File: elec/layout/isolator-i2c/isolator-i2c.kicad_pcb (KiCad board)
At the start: 2 copper layers, 7 parts, among them U1 10kΩ ±1% 62.5mW, U2 10kΩ ±1% 62.5mW, U4 10kΩ ±1% 62.5mW, U5 10kΩ ±1% 62.5mW, U6 100nF ±10% 16V X7R, U7 100nF ±10% 16V X7R

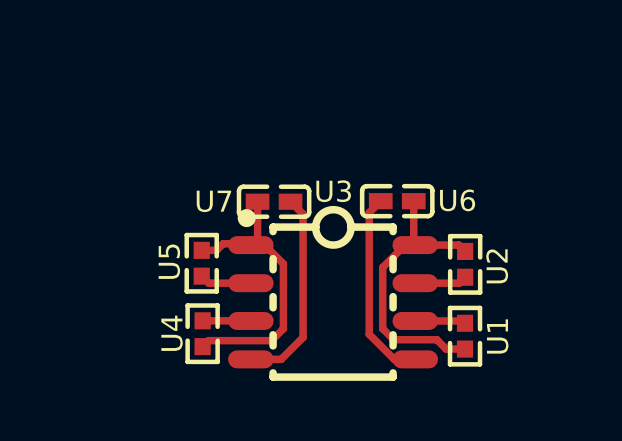
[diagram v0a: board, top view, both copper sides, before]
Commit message: remove default build, build everything locally
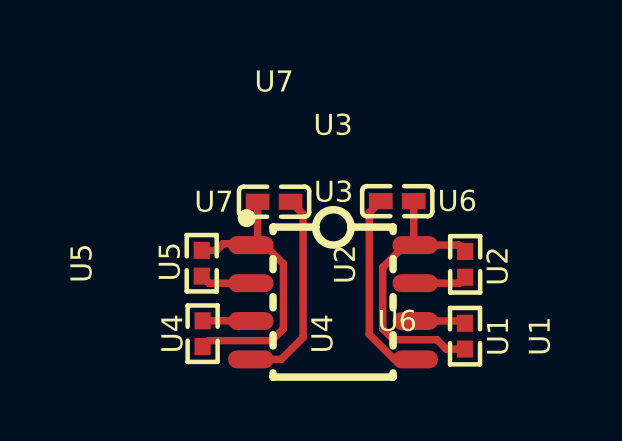
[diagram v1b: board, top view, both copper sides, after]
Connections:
- net scl renamed line-2
- net scl-1 renamed line-1
- net sda renamed line-3
- net sda-1 renamed line
- U1 pad 2: hv-1 -> hv
- U2 pad 2: hv-1 -> hv
- U3 pad 1: hv -> hv-1
- U3 pad 4: gnd -> gnd-1
- U3 pad 5: gnd-1 -> gnd
- U3 pad 8: hv-1 -> hv
- U4 pad 2: hv -> hv-1
- U5 pad 2: hv -> hv-1
- U6 pad 1: hv-1 -> hv
- U6 pad 2: gnd-1 -> gnd
- U7 pad 1: hv -> hv-1
- U7 pad 2: gnd -> gnd-1

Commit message: add module builds back in to ato.yaml with mfg-data excluded in config
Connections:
- U1 pad 1: line-1 -> line-3
- U2 pad 1: line-3 -> line-1
- U3 pad 2: line -> line-2
- U3 pad 3: line-2 -> line
- U3 pad 4: gnd-1 -> gnd
- U3 pad 5: gnd -> gnd-1
- U3 pad 6: line-1 -> line-3
- U3 pad 7: line-3 -> line-1
- U4 pad 1: line-2 -> line
- U5 pad 1: line -> line-2
- U6 pad 2: gnd -> gnd-1
- U7 pad 2: gnd-1 -> gnd
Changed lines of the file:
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@@
             (outputdirectory "")))
     (net 0 "")
-    (net 1 "line-3")
-    (net 2 "line-2")
+    (net 1 "line-1")
+    (net 2 "line")
     (net 3 "hv")
-    (net 4 "line")
-    (net 5 "line-1")
-    (net 6 "gnd-1")
+    (net 4 "line-2")
+    (net 5 "line-3")
+    (net 6 "gnd")
     (net 7 "hv-1")
-    (net 8 "gnd")
+    (net 8 "gnd-1")
     (footprint "atopile:R0402-56259e"
         (layer "F.Cu")
@@
             (layers "F.Cu" "F.Paste" "F.Mask")
             (remove_unused_layers no)
-            (net 1 "line-3"))
+            (net 1 "line-1"))
         (pad "2" smd rect
             (at 0.43 0 90)
@@
             (layers "F.Cu" "F.Paste" "F.Mask")
             (remove_unused_layers no)
-            (net 4 "line"))
+            (net 4 "line-2"))
         (pad "3" smd oval
             (at -2.74 0.63 90)
@@
             (layers "F.Cu" "F.Paste" "F.Mask")
             (remove_unused_layers no)
-            (net 2 "line-2"))
+            (net 2 "line"))
         (pad "4" smd oval
             (at -2.74 1.91 90)
@@
             (layers "F.Cu" "F.Paste" "F.Mask")
             (remove_unused_layers no)
-            (net 6 "gnd-1"))
+            (net 6 "gnd"))
         (pad "5" smd oval
             (at 2.74 1.91 90)
@@
             (layers "F.Cu" "F.Paste" "F.Mask")
             (remove_unused_layers no)
-            (net 8 "gnd"))
+            (net 8 "gnd-1"))
         (pad "6" smd oval
             (at 2.74 0.63 90)
@@
             (layers "F.Cu" "F.Paste" "F.Mask")
             (remove_unused_layers no)
-            (net 5 "line-1"))
+            (net 5 "line-3"))
         (pad "7" smd oval
             (at 2.74 -0.63 90)
@@
             (layers "F.Cu" "F.Paste" "F.Mask")
             (remove_unused_layers no)
-            (net 1 "line-3"))
+            (net 1 "line-1"))
         (pad "8" smd oval
             (at 2.74 -1.9 90)
@@
             (layers "F.Cu" "F.Paste" "F.Mask")
             (remove_unused_layers no)
-            (net 8 "gnd")))
+            (net 8 "gnd-1")))
     (footprint "atopile:C0402-b3ef17"
         (layer "F.Cu")
@@
             (layers "F.Cu" "F.Paste" "F.Mask")
             (remove_unused_layers no)
-            (net 6 "gnd-1")))
+            (net 6 "gnd")))
     (footprint "atopile:R0402-56259e"
         (layer "F.Cu")
@@
             (layers "F.Cu" "F.Paste" "F.Mask")
             (remove_unused_layers no)
-            (net 5 "line-1"))
+            (net 5 "line-3"))
         (pad "2" smd rect
             (at 0.43 0 270)
@@
             (layers "F.Cu" "F.Paste" "F.Mask")
             (remove_unused_layers no)
-            (net 4 "line"))
+            (net 4 "line-2"))
         (pad "2" smd rect
             (at 0.43 0 90)
@@
             (layers "F.Cu" "F.Paste" "F.Mask")
             (remove_unused_layers no)
-            (net 2 "line-2"))
+            (net 2 "line"))
         (pad "2" smd rect
             (at 0.43 0 270)

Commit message: add CAN isolator, cellsim cell
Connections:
- U1 pad 1: line-3 -> line-2
- U2 pad 1: line-1 -> line-3
- U3 pad 2: line-2 -> line
- U3 pad 3: line -> line-1
- U3 pad 6: line-3 -> line-2
- U3 pad 7: line-1 -> line-3
- U4 pad 1: line -> line-1
- U5 pad 1: line-2 -> line
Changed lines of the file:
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@@
             (outputdirectory "")))
     (net 0 "")
-    (net 1 "line-1")
-    (net 2 "line")
+    (net 1 "line-3")
+    (net 2 "line-1")
     (net 3 "hv")
-    (net 4 "line-2")
-    (net 5 "line-3")
+    (net 4 "line")
+    (net 5 "line-2")
     (net 6 "gnd")
     (net 7 "hv-1")
@@
             (layers "F.Cu" "F.Paste" "F.Mask")
             (remove_unused_layers no)
-            (net 1 "line-1"))
+            (net 1 "line-3"))
         (pad "2" smd rect
             (at 0.43 0 90)
@@
             (layers "F.Cu" "F.Paste" "F.Mask")
             (remove_unused_layers no)
-            (net 4 "line-2"))
+            (net 4 "line"))
         (pad "3" smd oval
             (at -2.74 0.63 90)
@@
             (layers "F.Cu" "F.Paste" "F.Mask")
             (remove_unused_layers no)
-            (net 2 "line"))
+            (net 2 "line-1"))
         (pad "4" smd oval
             (at -2.74 1.91 90)
@@
             (layers "F.Cu" "F.Paste" "F.Mask")
             (remove_unused_layers no)
-            (net 5 "line-3"))
+            (net 5 "line-2"))
         (pad "7" smd oval
             (at 2.74 -0.63 90)
@@
             (layers "F.Cu" "F.Paste" "F.Mask")
             (remove_unused_layers no)
-            (net 1 "line-1"))
+            (net 1 "line-3"))
         (pad "8" smd oval
             (at 2.74 -1.9 90)
@@
             (layers "F.Cu" "F.Paste" "F.Mask")
             (remove_unused_layers no)
-            (net 5 "line-3"))
+            (net 5 "line-2"))
         (pad "2" smd rect
             (at 0.43 0 270)
@@
             (layers "F.Cu" "F.Paste" "F.Mask")
             (remove_unused_layers no)
-            (net 4 "line-2"))
+            (net 4 "line"))
         (pad "2" smd rect
             (at 0.43 0 90)
@@
             (layers "F.Cu" "F.Paste" "F.Mask")
             (remove_unused_layers no)
-            (net 2 "line"))
+            (net 2 "line-1"))
         (pad "2" smd rect
             (at 0.43 0 270)

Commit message: rebuild all modules
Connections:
- U1 pad 1: line-2 -> line-3
- U1 pad 2: hv -> hv-1
- U2 pad 1: line-3 -> line-1
- U2 pad 2: hv -> hv-1
- U3 pad 1: hv-1 -> hv
- U3 pad 2: line -> line-2
- U3 pad 3: line-1 -> line
- U3 pad 6: line-2 -> line-3
- U3 pad 7: line-3 -> line-1
- U3 pad 8: hv -> hv-1
- U4 pad 1: line-1 -> line
- U4 pad 2: hv-1 -> hv
- U5 pad 1: line -> line-2
- U5 pad 2: hv-1 -> hv
- U6 pad 1: hv -> hv-1
- U7 pad 1: hv-1 -> hv
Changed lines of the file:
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@@
             (outputdirectory "")))
     (net 0 "")
-    (net 1 "line-3")
-    (net 2 "line-1")
-    (net 3 "hv")
-    (net 4 "line")
-    (net 5 "line-2")
+    (net 1 "line-1")
+    (net 2 "line")
+    (net 3 "hv-1")
+    (net 4 "line-2")
+    (net 5 "line-3")
     (net 6 "gnd")
-    (net 7 "hv-1")
+    (net 7 "hv")
     (net 8 "gnd-1")
     (footprint "atopile:R0402-56259e"
@@
             (layers "F.Cu" "F.Paste" "F.Mask")
             (remove_unused_layers no)
-            (net 1 "line-3"))
+            (net 1 "line-1"))
         (pad "2" smd rect
             (at 0.43 0 90)
@@
             (layers "F.Cu" "F.Paste" "F.Mask")
             (remove_unused_layers no)
-            (net 3 "hv")))
+            (net 3 "hv-1")))
     (footprint "lib:SOIC-8_L4.9-W3.9-P1.27-LS6.0-TL"
         (layer "F.Cu")
@@
             (layers "F.Cu" "F.Paste" "F.Mask")
             (remove_unused_layers no)
-            (net 7 "hv-1"))
+            (net 7 "hv"))
         (pad "2" smd oval
             (at -2.74 -0.63 90)
@@
             (layers "F.Cu" "F.Paste" "F.Mask")
             (remove_unused_layers no)
-            (net 4 "line"))
+            (net 4 "line-2"))
         (pad "3" smd oval
             (at -2.74 0.63 90)
@@
             (layers "F.Cu" "F.Paste" "F.Mask")
             (remove_unused_layers no)
-            (net 2 "line-1"))
+            (net 2 "line"))
         (pad "4" smd oval
             (at -2.74 1.91 90)
@@
             (layers "F.Cu" "F.Paste" "F.Mask")
             (remove_unused_layers no)
-            (net 5 "line-2"))
+            (net 5 "line-3"))
         (pad "7" smd oval
             (at 2.74 -0.63 90)
@@
             (layers "F.Cu" "F.Paste" "F.Mask")
             (remove_unused_layers no)
-            (net 1 "line-3"))
+            (net 1 "line-1"))
         (pad "8" smd oval
             (at 2.74 -1.9 90)
@@
             (layers "F.Cu" "F.Paste" "F.Mask")
             (remove_unused_layers no)
-            (net 3 "hv"))
+            (net 3 "hv-1"))
         (model "/Users/narayanpowderly/projects/hil-blocks/build/footprints/footprints.3dshapes/SOIC-8_L4.9-W3.9-H1.7-LS6.0-P1.27.step"
             (offset
@@
             (layers "F.Cu" "F.Paste" "F.Mask")
             (remove_unused_layers no)
-            (net 3 "hv"))
+            (net 3 "hv-1"))
         (pad "2" smd rect
             (at 0.55 0 180)
@@
             (layers "F.Cu" "F.Paste" "F.Mask")
             (remove_unused_layers no)
-            (net 7 "hv-1"))
+            (net 7 "hv"))
         (pad "2" smd rect
             (at 0.55 0 0)
@@
             (layers "F.Cu" "F.Paste" "F.Mask")
             (remove_unused_layers no)
-            (net 5 "line-2"))
+            (net 5 "line-3"))
         (pad "2" smd rect
             (at 0.43 0 270)
@@
             (layers "F.Cu" "F.Paste" "F.Mask")
             (remove_unused_layers no)
-            (net 3 "hv")))
+            (net 3 "hv-1")))
     (footprint "atopile:R0402-56259e"
         (layer "F.Cu")
@@
             (layers "F.Cu" "F.Paste" "F.Mask")
             (remove_unused_layers no)
-            (net 4 "line"))
+            (net 4 "line-2"))
         (pad "2" smd rect
             (at 0.43 0 90)
@@
             (layers "F.Cu" "F.Paste" "F.Mask")
             (remove_unused_layers no)
-            (net 7 "hv-1")))
+            (net 7 "hv")))
     (footprint "atopile:R0402-56259e"
         (layer "F.Cu")
@@
             (layers "F.Cu" "F.Paste" "F.Mask")
             (remove_unused_layers no)
-            (net 2 "line-1"))
+            (net 2 "line"))
         (pad "2" smd rect
             (at 0.43 0 270)
@@
             (layers "F.Cu" "F.Paste" "F.Mask")
             (remove_unused_layers no)
-            (net 7 "hv-1")))
+            (net 7 "hv")))
     (segment
         (start 152.24 99.87)

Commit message: core layout, rebuild modules with compiler updates
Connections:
- U1 pad 1: line-3 -> line-2
- U2 pad 1: line-1 -> line-3
- U3 pad 2: line-2 -> line-1
- U3 pad 6: line-3 -> line-2
- U3 pad 7: line-1 -> line-3
- U5 pad 1: line-2 -> line-1
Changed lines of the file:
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@@
             (outputdirectory "")))
     (net 0 "")
-    (net 1 "line-1")
+    (net 1 "line-3")
     (net 2 "line")
     (net 3 "hv-1")
-    (net 4 "line-2")
-    (net 5 "line-3")
+    (net 4 "line-1")
+    (net 5 "line-2")
     (net 6 "gnd")
     (net 7 "hv")
@@
             (layers "F.Cu" "F.Paste" "F.Mask")
             (remove_unused_layers no)
-            (net 1 "line-1"))
+            (net 1 "line-3"))
         (pad "2" smd rect
             (at 0.43 0 90)
@@
             (layers "F.Cu" "F.Paste" "F.Mask")
             (remove_unused_layers no)
-            (net 4 "line-2"))
+            (net 4 "line-1"))
         (pad "3" smd oval
             (at -2.74 0.63 90)
@@
             (layers "F.Cu" "F.Paste" "F.Mask")
             (remove_unused_layers no)
-            (net 5 "line-3"))
+            (net 5 "line-2"))
         (pad "7" smd oval
             (at 2.74 -0.63 90)
@@
             (layers "F.Cu" "F.Paste" "F.Mask")
             (remove_unused_layers no)
-            (net 1 "line-1"))
+            (net 1 "line-3"))
         (pad "8" smd oval
             (at 2.74 -1.9 90)
@@
             (layers "F.Cu" "F.Paste" "F.Mask")
             (remove_unused_layers no)
-            (net 5 "line-3"))
+            (net 5 "line-2"))
         (pad "2" smd rect
             (at 0.43 0 270)
@@
             (layers "F.Cu" "F.Paste" "F.Mask")
             (remove_unused_layers no)
-            (net 4 "line-2"))
+            (net 4 "line-1"))
         (pad "2" smd rect
             (at 0.43 0 90)

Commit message: Everything builds
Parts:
- U1, U2, U4, U5: value 10kΩ ±1% 62.5mW -> 1kΩ ±1% 62.5mW
- U3: footprint lib:SOIC-8_L4.9-W3.9-P1.27-LS6.0-TL -> atopile:SOIC-8_L4.9-W3.9-P1.27-LS6.0-TL-e13595
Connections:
- U1 pad 1: line-2 -> line-1
- U1 pad 2: hv-1 -> hv
- U2 pad 2: hv-1 -> hv
- U3 pad 1: hv -> hv-1
- U3 pad 2: line-1 -> line-2
- U3 pad 6: line-2 -> line-1
- U3 pad 8: hv-1 -> hv
- U4 pad 2: hv -> hv-1
- U5 pad 1: line-1 -> line-2
- U5 pad 2: hv -> hv-1
- U6 pad 1: hv-1 -> hv
- U7 pad 1: hv -> hv-1
